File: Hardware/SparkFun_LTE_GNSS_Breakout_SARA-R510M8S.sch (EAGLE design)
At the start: 158 parts, among them IC1 SN74AVC4T774PW, IC2 SN74AVC4T774PW, J13 TP, J17 NANO_SIM, J19 NI, Q1 310mA/60V/1.6Ω, Q2 310mA/60V/1.6Ω, Q3 310mA/60V/1.6Ω, Q4 310mA/60V/1.6Ω, Q5 20V/0.2A/8MHz/1.2Ω/1Vth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

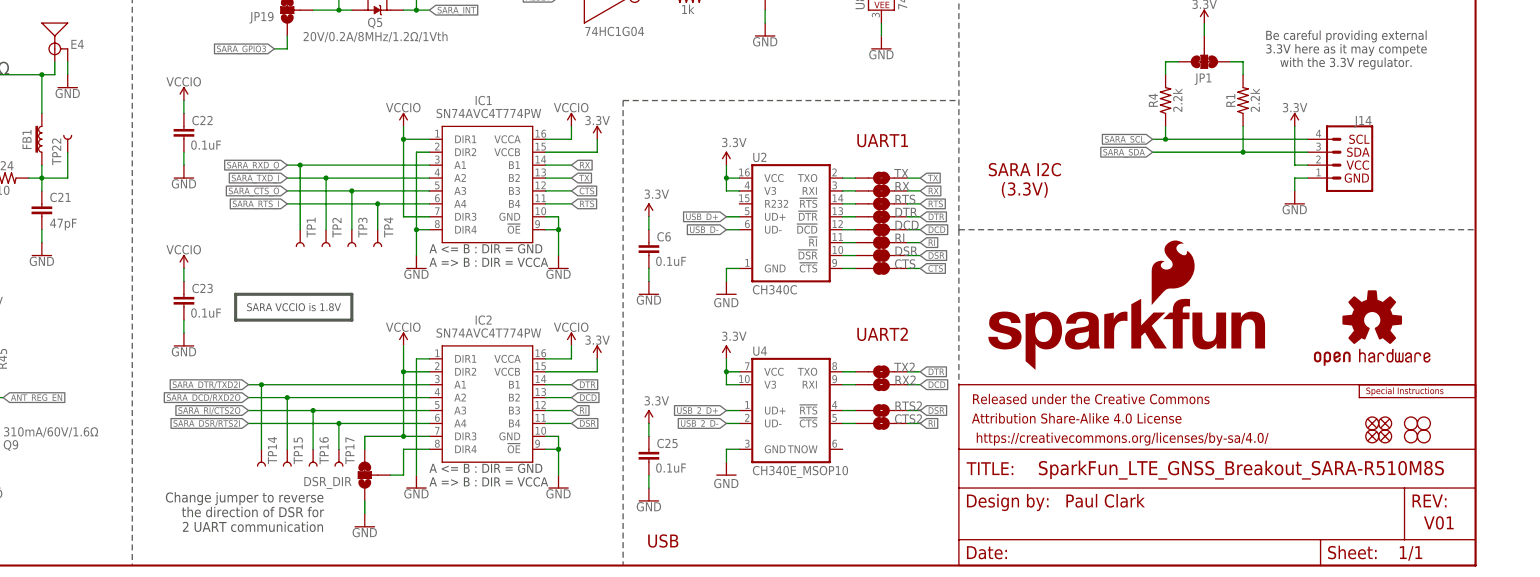
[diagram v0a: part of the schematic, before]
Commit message: V10
Added 100k Pulldown resistors to RTS and DTR
Moved "L1" label from the top of the board to the bottom
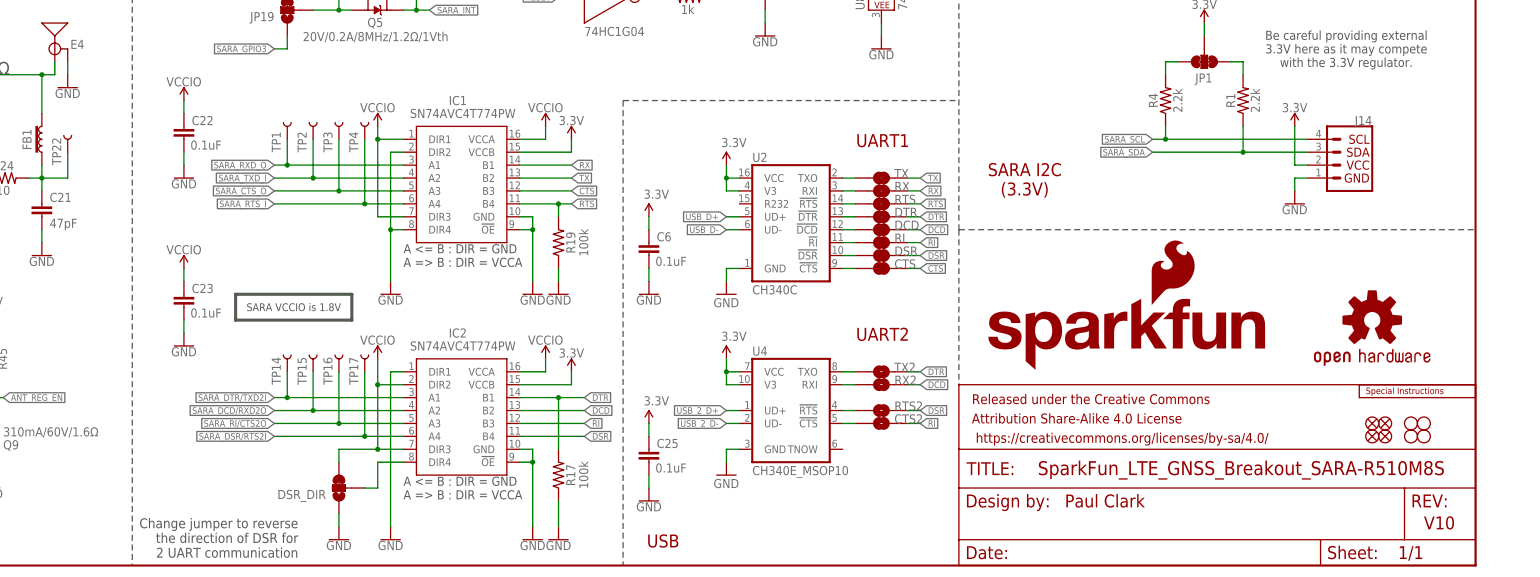
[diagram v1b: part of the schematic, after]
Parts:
- added R17, R19: 100k, SparkFun-Resistors:100KOHM-0603-1/10W-1%
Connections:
- net DTR: now also R17.2
- net GND: now also R17.1, R19.1
- net RTS: now also R19.2
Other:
- note added: "V10"
- note removed: "V01"
- moved on the sheet: DSR_DIR, IC1, IC2, TP1, TP14, TP15, TP16, TP17, TP2, TP3, TP4

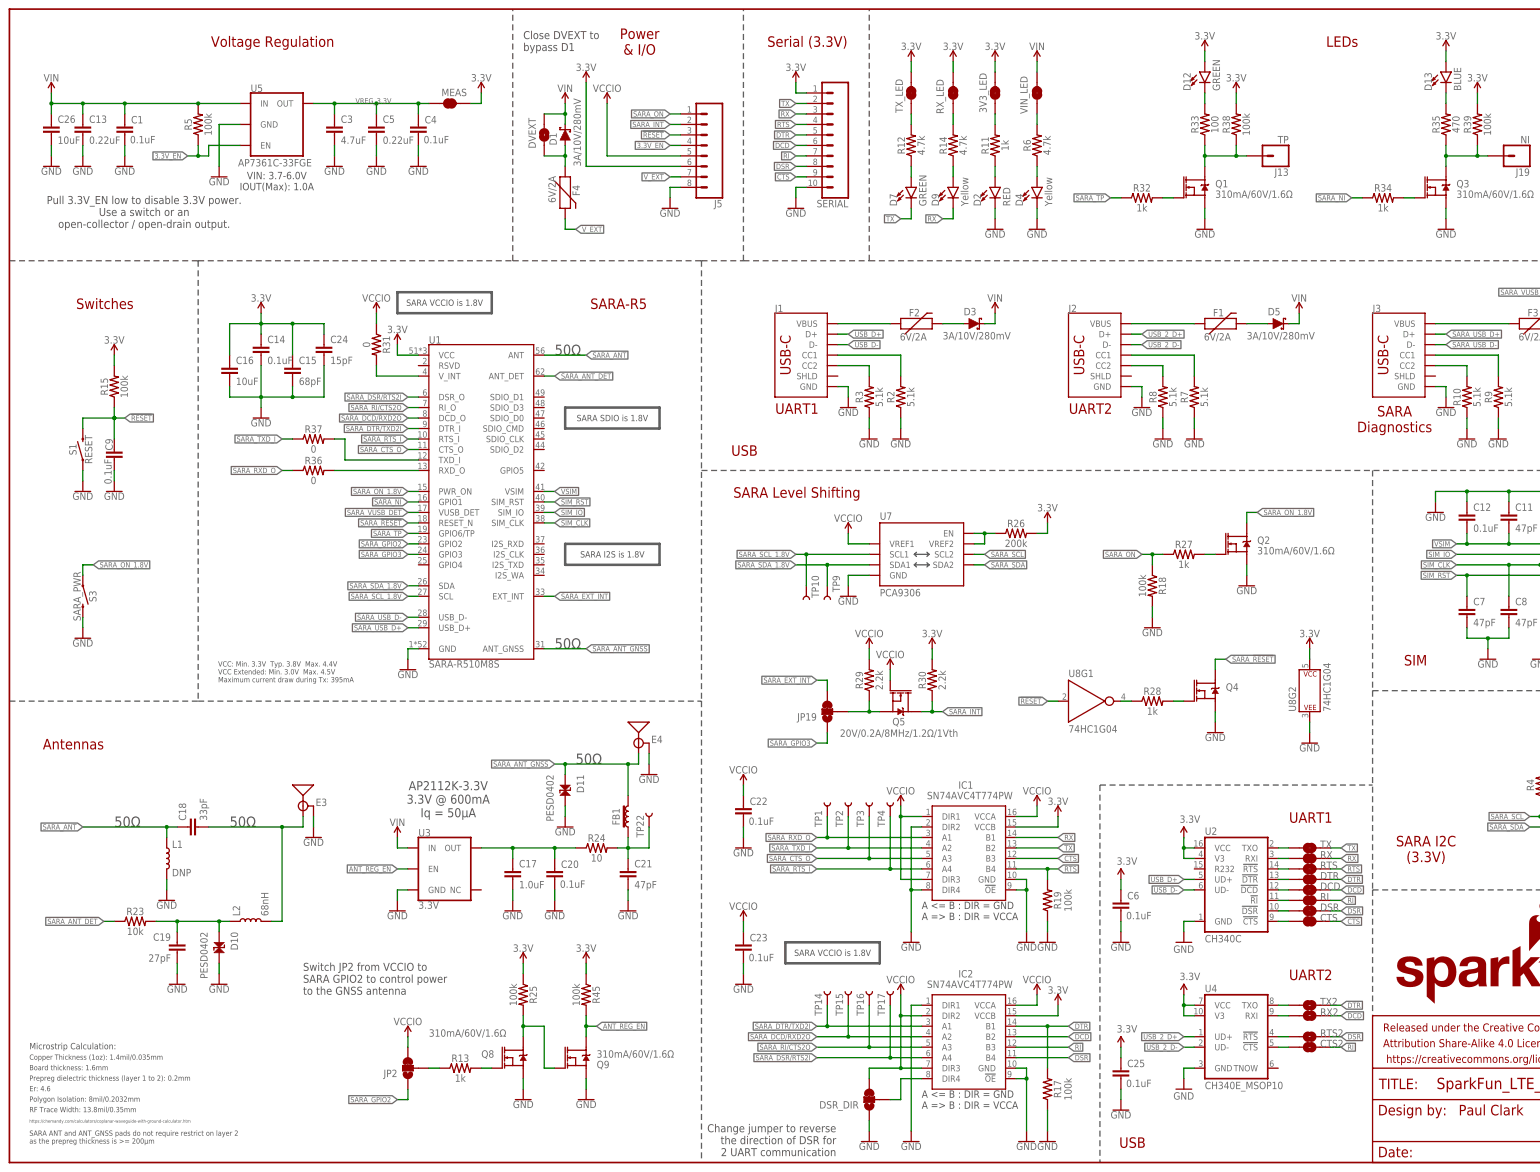
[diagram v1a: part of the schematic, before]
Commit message: V10 design review changes
-Updated Schematic PDF
-Added new parts to sparkfun libraries
-Fixed labels for schematic sections
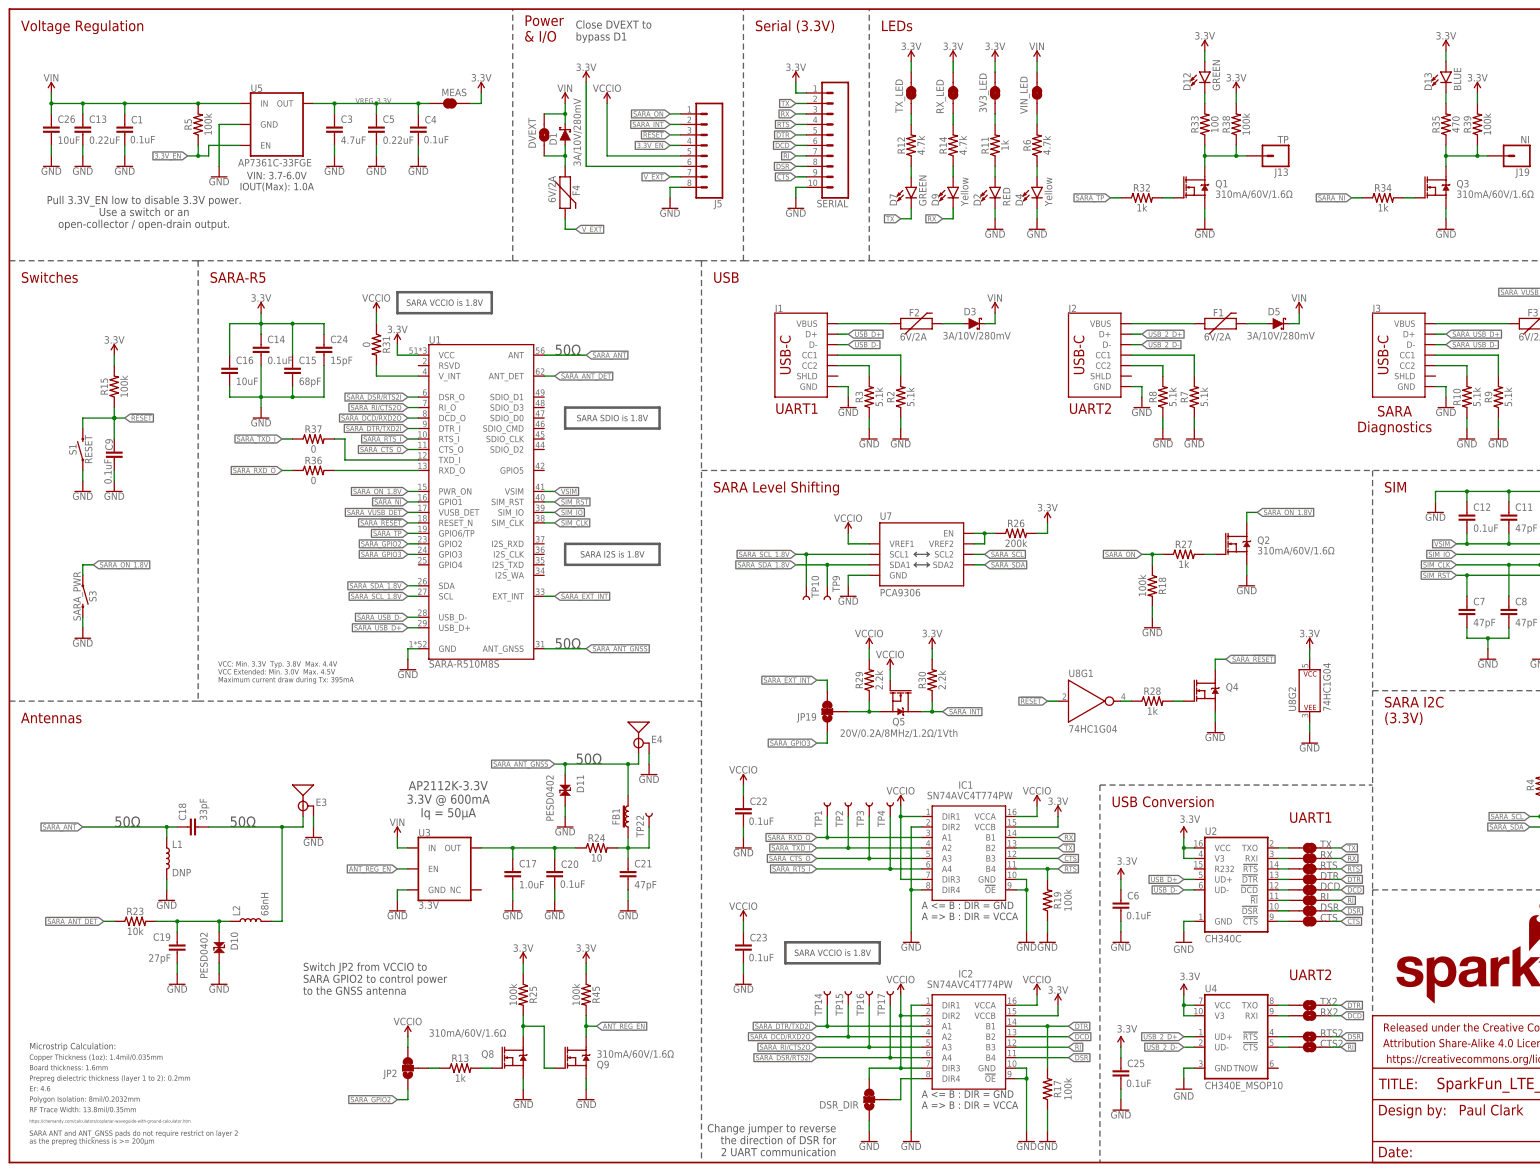
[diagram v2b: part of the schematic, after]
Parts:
- C18: device New_Parts:33PF-0402-25V-5%-X7R -> SparkFun-Capacitors:33PF-0402T-50V-5%
- C19: device New_Parts:27PF-0402-25V-5%-X7R -> SparkFun-Capacitors:27PF-0402-50V-5%
- D10, D11: device New_Parts:PESD0402 -> SparkFun-DiscreteSemi:PESD0402
- IC1, IC2: device New_Parts:SN74AVC4T774PW -> SparkFun-IC-Comms:SN74AVC4T774PW
- L1: device New_Parts:INDUCTOR_DNP-0402 -> SparkFun-Coils:INDUCTORDNP-0402-COILCRAFT
- L2: device New_Parts:68NH-0402 -> SparkFun-Coils:68NH-0402
- U1: device SARA_R5:SARA-R510M8S -> SparkFun-RF:SARA-R510M8S
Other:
- note added: "USB Conversion"
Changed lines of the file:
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@@
 <?xml version="1.0" encoding="utf-8"?>
 <!DOCTYPE eagle SYSTEM "eagle.dtd">
-<eagle version="9.6.2">
+<eagle version="9.5.2">
 <drawing>
 <settings>
@@
 <part name="SUPPLY29" library="SparkFun-PowerSymbols" deviceset="3.3V" device=""/>
 <part name="GND41" library="SparkFun-PowerSymbols" deviceset="GND" device=""/>
-<part name="U1" library="SARA_R5" deviceset="SARA-R510M8S" device="" value="SARA-R510M8S"/>
+<part name="U1" library="SparkFun-RF" deviceset="SARA-R510M8S" device="" value="SARA-R510M8S"/>
 <part name="GND31" library="SparkFun-PowerSymbols" deviceset="GND" device=""/>
 <part name="GND32" library="SparkFun-PowerSymbols" deviceset="GND" device=""/>
@@
 <part name="GND39" library="SparkFun-PowerSymbols" deviceset="GND" device=""/>
 <part name="C16" library="SparkFun-Capacitors" deviceset="10UF" device="-0603-6.3V-20%" value="10uF"/>
-<part name="L2" library="New_Parts" deviceset="68NH" device="-0402" value="68nH"/>
-<part name="L1" library="New_Parts" deviceset="INDUCTOR_DNP" device="-0402" value="DNP"/>
+<part name="L2" library="SparkFun-Coils" deviceset="68NH" device="-0402" value="68nH"/>
+<part name="L1" library="SparkFun-Coils" deviceset="INDUCTOR" device="DNP-0402-COILCRAFT" value="DNP"/>
 <part name="GND45" library="SparkFun-PowerSymbols" deviceset="GND" device=""/>
-<part name="C18" library="New_Parts" deviceset="33PF" device="-0402-25V-5%-X7R" value="33pF"/>
-<part name="C19" library="New_Parts" deviceset="27PF" device="-0402-25V-5%-X7R" value="27pF"/>
+<part name="C18" library="SparkFun-Capacitors" deviceset="33PF" device="-0402T-50V-5%" value="33pF"/>
+<part name="C19" library="SparkFun-Capacitors" deviceset="27PF" device="-0402-50V-5%" value="27pF"/>
 <part name="R23" library="SparkFun-Resistors" deviceset="10KOHM" device="-0603-1/10W-1%" value="10k"/>
 <part name="GND46" library="SparkFun-PowerSymbols" deviceset="GND" device=""/>
-<part name="D10" library="New_Parts" deviceset="PESD0402" device=""/>
+<part name="D10" library="SparkFun-DiscreteSemi" deviceset="PESD0402" device=""/>
 <part name="GND50" library="SparkFun-PowerSymbols" deviceset="GND" device=""/>
 <part name="U3" library="SparkFun-IC-Power" deviceset="V_REG_AP2112" device="K-3.3V" value="3.3V"/>
@@
 <part name="GND54" library="SparkFun-PowerSymbols" deviceset="GND" device=""/>
 <part name="R25" library="SparkFun-Resistors" deviceset="100KOHM" device="-0603-1/10W-1%" value="100k"/>
-<part name="D11" library="New_Parts" deviceset="PESD0402" device=""/>
+<part name="D11" library="SparkFun-DiscreteSemi" deviceset="PESD0402" device=""/>
 <part name="GND57" library="SparkFun-PowerSymbols" deviceset="GND" device=""/>
 <part name="SUPPLY24" library="SparkFun-PowerSymbols" deviceset="VCCIO" device=""/>
@@
 <part name="TP22" library="SparkFun-Connectors" deviceset="TEST-POINT" device="3" value="TEST-POINT3"/>
 <part name="C24" library="SparkFun-Capacitors" deviceset="15PF" device="-0603-50V-5%" value="15pF"/>
-<part name="IC1" library="New_Parts" deviceset="SN74AVC4T774PW" device=""/>
+<part name="IC1" library="SparkFun-IC-Comms" deviceset="SN74AVC4T774PW" device="" value="SN74AVC4T774PW"/>
 <part name="GND56" library="SparkFun-PowerSymbols" deviceset="GND" device=""/>
 <part name="GND70" library="SparkFun-PowerSymbols" deviceset="GND" device=""/>
 <part name="SUPPLY55" library="SparkFun-PowerSymbols" deviceset="VCCIO" device=""/>
 <part name="SUPPLY56" library="SparkFun-PowerSymbols" deviceset="VCCIO" device=""/>
-<part name="IC2" library="New_Parts" deviceset="SN74AVC4T774PW" device=""/>
+<part name="IC2" library="SparkFun-IC-Comms" deviceset="SN74AVC4T774PW" device="" value="SN74AVC4T774PW"/>
 <part name="SUPPLY57" library="SparkFun-PowerSymbols" deviceset="VCCIO" device=""/>
 <part name="SUPPLY58" library="SparkFun-PowerSymbols" deviceset="3.3V" device=""/>
@@
 <sheet>
 <plain>
-<text x="178.054" y="172.466" size="2.54" layer="94" font="vector" align="center">USB</text>
-<text x="63.754" y="271.526" size="2.54" layer="94" font="vector" align="center">Voltage Regulation</text>
+<text x="170.434" y="213.106" size="2.54" layer="94" font="vector">USB</text>
+<text x="2.794" y="274.066" size="2.54" layer="94" font="vector">Voltage Regulation</text>
 <wire x1="0" y1="218.44" x2="45.72" y2="218.44" width="0.2032" layer="97" style="longdash"/>
 <wire x1="45.72" y1="218.44" x2="121.92" y2="218.44" width="0.2032" layer="97" style="longdash"/>
@@
 <text x="64.77" y="237.744" size="1.778" layer="97" font="vector" align="center">VIN: 3.7-6.0V
 IOUT(Max): 1.0A</text>
-<text x="322.834" y="271.526" size="2.54" layer="94" font="vector" align="center">LEDs</text>
+<text x="211.074" y="274.066" size="2.54" layer="94" font="vector">LEDs</text>
 <wire x1="330.2" y1="114.3" x2="330.2" y2="66.04" width="0.2032" layer="97" style="longdash"/>
 <wire x1="330.2" y1="66.04" x2="330.2" y2="35.56" width="0.2032" layer="97" style="longdash"/>
-<text x="23.114" y="208.026" size="2.54" layer="94" font="vector" align="center">Switches</text>
-<text x="147.574" y="208.026" size="2.54" layer="94" font="vector" align="center">SARA-R5</text>
+<text x="2.794" y="213.106" size="2.54" layer="94" font="vector">Switches</text>
+<text x="48.514" y="213.106" size="2.54" layer="94" font="vector">SARA-R5</text>
 <wire x1="45.72" y1="111.76" x2="167.64" y2="111.76" width="0.2032" layer="97" style="longdash"/>
 <wire x1="0" y1="111.76" x2="45.72" y2="111.76" width="0.2032" layer="97" style="longdash"/>
 <wire x1="330.2" y1="66.04" x2="431.8" y2="66.04" width="0.2032" layer="97" style="longdash"/>
 <wire x1="167.64" y1="167.64" x2="431.8" y2="167.64" width="0.2032" layer="97" style="longdash"/>
-<text x="340.614" y="121.666" size="2.54" layer="94" font="vector" align="center">SIM</text>
+<text x="332.994" y="162.306" size="2.54" layer="94" font="vector">SIM</text>
 <text x="146.05" y="181.102" size="1.524" layer="97" font="vector" ratio="15" rot="R180" align="bottom-center">SARA SDIO is 1.8V</text>
 <wire x1="157.48" y1="177.8" x2="134.62" y2="177.8" width="0.6096" layer="97"/>
@@
 <wire x1="134.62" y1="149.86" x2="157.48" y2="149.86" width="0.6096" layer="97"/>
 <wire x1="157.48" y1="149.86" x2="157.48" y2="144.78" width="0.6096" layer="97"/>
-<text x="152.654" y="271.526" size="2.54" layer="94" font="vector" align="center">Power
+<text x="124.714" y="271.526" size="2.54" layer="94" font="vector">Power
 &amp; I/O</text>
-<text x="343.154" y="75.946" size="2.54" layer="94" font="vector" align="center">SARA I2C
+<text x="332.994" y="106.426" size="2.54" layer="94" font="vector">SARA I2C
 (3.3V)</text>
 <text x="406.4" y="101.6" size="1.778" layer="97" font="vector" align="center">Be careful providing external
@@
 <text x="25.4" y="81.28" size="2.54" layer="97" font="vector">50Ω</text>
 <text x="53.34" y="81.28" size="2.54" layer="97" font="vector">50Ω</text>
-<text x="15.494" y="101.346" size="2.54" layer="94" font="vector" align="center">Antennas</text>
+<text x="2.794" y="106.426" size="2.54" layer="94" font="vector">Antennas</text>
 <text x="50.546" y="121.412" size="1.27" layer="97" font="vector" align="top-left">VCC: Min. 3.3V  Typ. 3.8V  Max. 4.4V
 VCC Extended: Min. 3.0V  Max. 4.5V
@@
 Iq = 50µA </text>
 <wire x1="330.2" y1="114.3" x2="431.8" y2="114.3" width="0.2032" layer="97" style="longdash"/>
-<text x="190.754" y="162.306" size="2.54" layer="94" font="vector" align="center">SARA Level Shifting</text>
+<text x="170.434" y="162.306" size="2.54" layer="94" font="vector">SARA Level Shifting</text>
 <text x="200.279" y="9.271" size="1.9304" layer="97" font="vector" align="top-right">Change jumper to reverse
 the direction of DSR for
@@
 <wire x1="264.16" y1="91.44" x2="264.16" y2="0" width="0.2032" layer="97" style="longdash"/>
 <wire x1="264.16" y1="91.44" x2="330.2" y2="91.44" width="0.2032" layer="97" style="longdash"/>
-<text x="272.034" y="4.826" size="2.54" layer="94" font="vector" align="center">USB</text>
+<text x="266.954" y="86.106" size="2.54" layer="94" font="vector">USB Conversion</text>
 <wire x1="208.28" y1="218.44" x2="208.28" y2="279.4" width="0.2032" layer="97" style="longdash"/>
-<text x="193.294" y="271.526" size="2.54" layer="94" font="vector" align="center">Serial (3.3V)</text>
+<text x="180.594" y="274.066" size="2.54" layer="94" font="vector">Serial (3.3V)</text>
 <wire x1="177.8" y1="218.44" x2="177.8" y2="279.4" width="0.2032" layer="97" style="longdash"/>
 <text x="190.754" y="182.626" size="2.54" layer="94" font="vector" align="center">UART1</text>
@@
 Use a switch or an
 open-collector / open-drain output.</text>
-<text x="124.46" y="269.24" size="1.9304" layer="97" font="vector">Close DVEXT to
+<text x="137.16" y="271.78" size="1.9304" layer="97" font="vector">Close DVEXT to
 bypass D1</text>
 <text x="71.12" y="40.64" size="1.9304" layer="97" font="vector">Switch JP2 from VCCIO to
